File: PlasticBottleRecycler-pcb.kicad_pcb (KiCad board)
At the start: 2 copper layers, 70.9 x 56.9 mm, 33 parts, among them J1 SWIM, J2 LCD, J3 Screw_Terminal_01x04, J4 NTC, J5 HEATER, J6 FAN1, J7 +12V, J8 +5V, Q1 IRF3205, Q2 BC337, SW1 RESET, SW2 SW_Push, SW3 SW_Push, SW4 SW_Push, U1 STM8S005K6T6C, U2 AMS1117

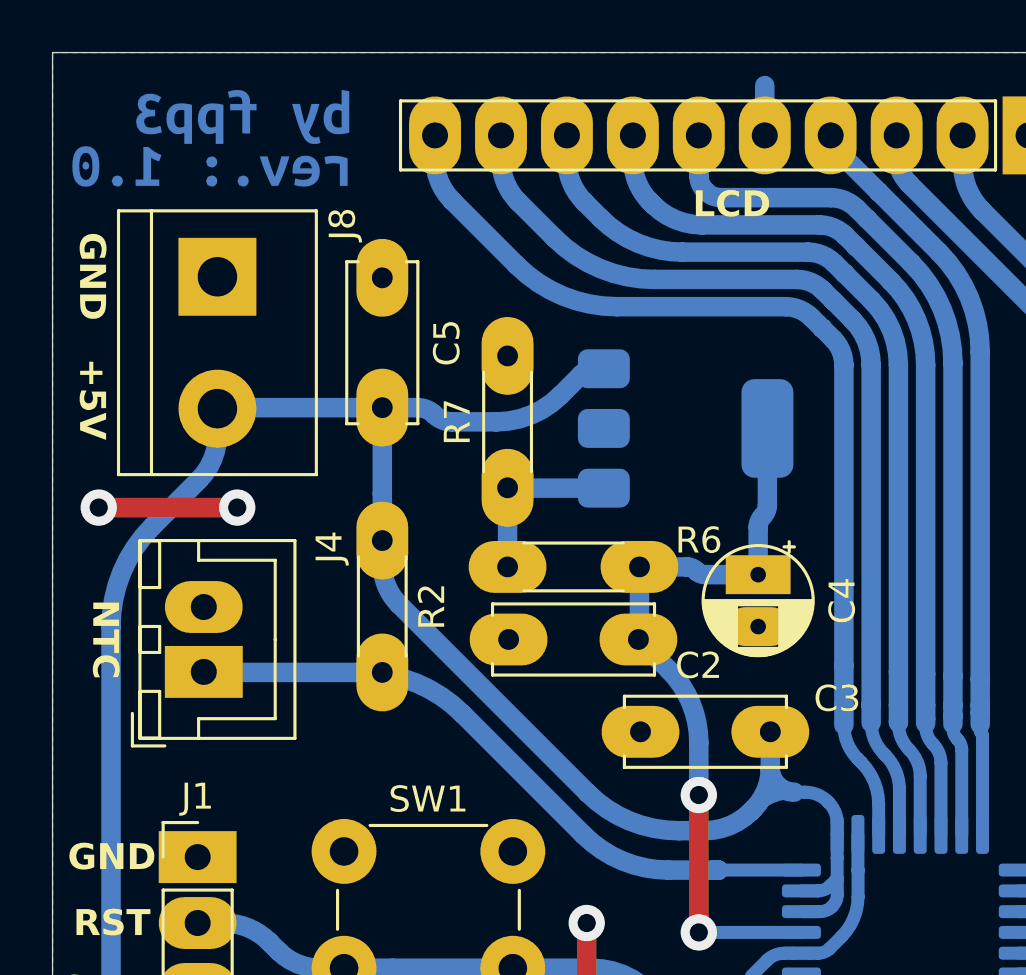
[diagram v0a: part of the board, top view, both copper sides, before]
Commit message: Remove unnecesary voltage regulator
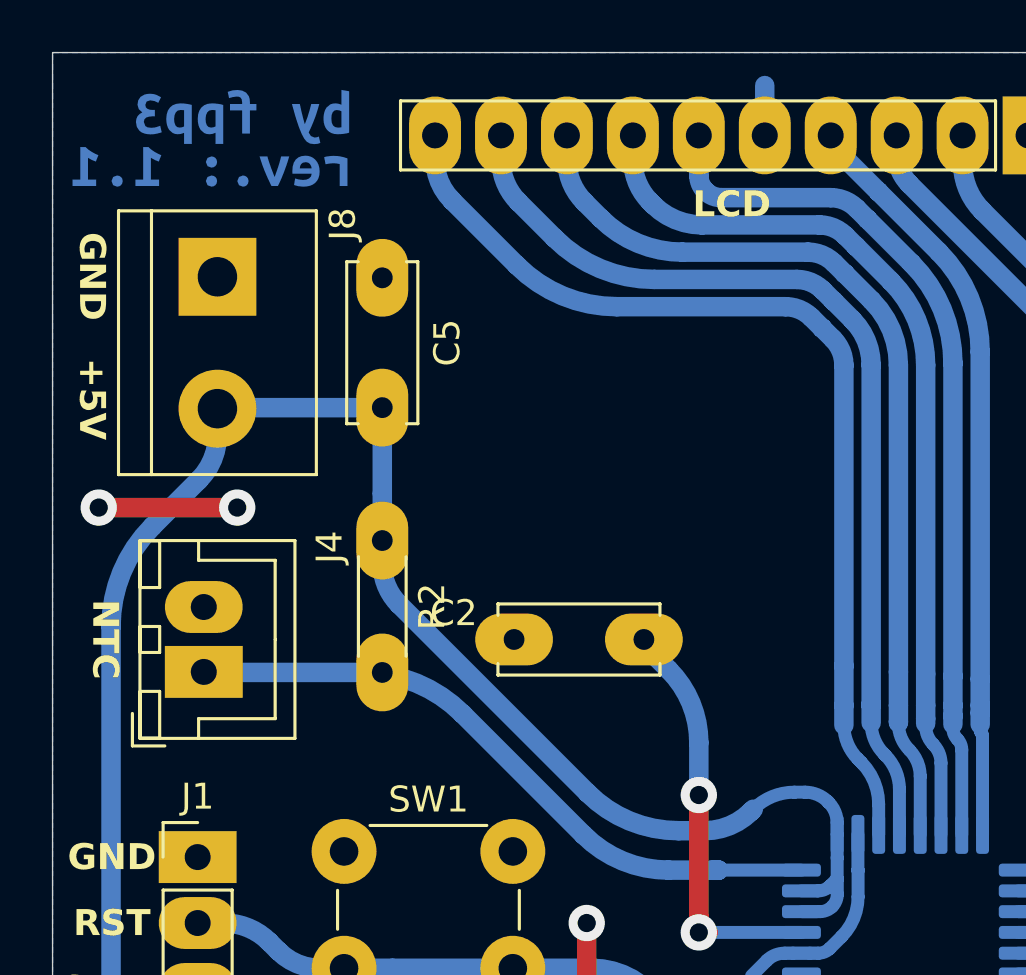
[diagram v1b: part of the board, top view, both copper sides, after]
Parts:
- removed C3: 100n, Capacitor_THT:C_Disc_D6.0mm_W2.5mm_P5.00mm
- removed C4: 10u, Capacitor_THT:CP_Radial_D4.0mm_P2.00mm
- removed R6: 10K, Resistor_THT:R_Axial_DIN0204_L3.6mm_D1.6mm_P5.08mm_Horizontal
- removed R7: 4K7, Resistor_THT:R_Axial_DIN0204_L3.6mm_D1.6mm_P5.08mm_Horizontal
- removed U2: AMS1117, Package_TO_SOT_SMD:SOT-223-3_TabPin2
- removed kibuzzard-679459C7: G***, kibuzzard-679459C7
- added kibuzzard-67C1DC92: G***, kibuzzard-67C1DC92, B.Cu at (121.2, 75.4)
- moved C2 5.21 mm to (137.9, 94.7), turned to 180 degrees
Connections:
- C2 pad 1: GND -> Net-(U1-VCAP)
- C2 pad 2: +1V8 -> GND
- U1 pad 5: +1V8 -> Net-(U1-VCAP)
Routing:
- net +1V8: track 29.7 -> 0.00 mm, vias 2 -> 0
- net Net-(U1-VCAP): track 0.00 -> 15.8 mm, vias 0 -> 2
- net +5V: track 269.8 -> 256.0 mm
- net Net-(U2-ADJ): track 7.53 -> 0.00 mm

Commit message: Revision 2.0
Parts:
- removed R8: 680, Resistor_THT:R_Axial_DIN0207_L6.3mm_D2.5mm_P10.16mm_Horizontal
- removed kibuzzard-679458C4: G***, kibuzzard-679458C4
- removed kibuzzard-67C1DC92: G***, kibuzzard-67C1DC92
- added BZ1: Buzzer, Buzzer_Beeper:Buzzer_12x9.5RM7.6, F.Cu at (124.3, 140.2)
- added C3: 100nF, Capacitor_THT:C_Disc_D6.0mm_W2.5mm_P5.00mm, F.Cu at (130.9, 118.0)
- added C4: 100n, Capacitor_THT:C_Disc_D6.0mm_W2.5mm_P5.00mm, F.Cu at (138.7, 131.5)
- added H1: MountingHole, MountingHole:MountingHole_3.2mm_M3, F.Cu at (133.1, 40.9)
- added H2: MountingHole, MountingHole:MountingHole_3.2mm_M3, F.Cu at (165.5, 40.9)
- added H3: MountingHole, MountingHole:MountingHole_3.2mm_M3, F.Cu at (124.8, 79.0)
- added H4: MountingHole, MountingHole:MountingHole_3.2mm_M3, F.Cu at (173.7, 79.0)
- added J10: RUNOUT, Connector_Molex:Molex_KK-254_AE-6410-03A_1x03_P2.54mm_Vertical, F.Cu at (178.9, 150.2)
- added J11: STEPPER, Connector_JST:JST_XA_B04B-XASK-1_1x04_P2.50mm_Vertical, F.Cu at (179.7, 140.6)
- added J12: LCD, Connector_PinHeader_2.54mm:PinHeader_1x10_P2.54mm_Vertical, B.Cu at (162.5, 51.3)
- added J9: NTC, Connector_JST:JST_XH_B2B-XH-A_1x02_P2.50mm_Vertical, F.Cu at (165.3, 150.1)
- added Q3: IRF3205, Package_TO_SOT_THT:TO-220-3_Vertical, F.Cu at (162.7, 107.6)
- added R6: 10K, Resistor_THT:R_Axial_DIN0204_L3.6mm_D1.6mm_P5.08mm_Horizontal, F.Cu at (147.5, 72.3)
- added R7: 10K, Resistor_THT:R_Axial_DIN0204_L3.6mm_D1.6mm_P5.08mm_Horizontal, F.Cu at (133.9, 72.3)
- added U2: STM8S005K6T6C, Package_QFP:LQFP-32_7x7mm_P0.8mm, B.Cu at (146.9, 134.4)
- added kibuzzard-67C39444: G***, kibuzzard-67C39444, B.Cu at (117.2, 107.6)
- added kibuzzard-67C39444: G***, kibuzzard-67C39444, B.Cu at (156.7, 44.2)
- added kibuzzard-67C39452: G***, kibuzzard-67C39452, B.Cu at (117.2, 147.1)
- added kibuzzard-67C39452: G***, kibuzzard-67C39452, B.Cu at (154.4, 39.8)
- added kibuzzard-67C3947F: G***, kibuzzard-67C3947F, B.Cu at (179.8, 104.2)
- added kibuzzard-67C3B0C4: G***, kibuzzard-67C3B0C4, B.Cu at (150.1, 83.9)
- C1: value 1000u -> 330nF; footprint Capacitor_THT:CP_Radial_D10.0mm_P5.00mm -> Capacitor_THT:C_Disc_D6.0mm_W2.5mm_P5.00mm
- C2: value 100n -> 1000u; footprint Capacitor_THT:C_Disc_D6.0mm_W2.5mm_P5.00mm -> Capacitor_THT:CP_Radial_D10.0mm_P5.00mm
- J1: value SWIM -> Conn_01x08; footprint Connector_PinHeader_2.54mm:PinHeader_1x04_P2.54mm_Vertical -> Connector_Molex:Molex_KK-254_AE-6410-08A_1x08_P2.54mm_Vertical
- J2: value LCD -> Conn_01x04; footprint Connector_PinHeader_2.54mm:PinHeader_1x10_P2.54mm_Vertical -> Connector_Molex:Molex_KK-254_AE-6410-04A_1x04_P2.54mm_Vertical
- J3: value Screw_Terminal_01x04 -> Conn_01x08; footprint TerminalBlock:TerminalBlock_bornier-4_P5.08mm -> Connector_Molex:Molex_KK-254_AE-6410-08A_1x08_P2.54mm_Vertical
- J4: value NTC -> Conn_01x04; footprint Connector_JST:JST_XH_B2B-XH-A_1x02_P2.50mm_Vertical -> Connector_Molex:Molex_KK-254_AE-6410-04A_1x04_P2.54mm_Vertical
- J5: value HEATER -> SWIM; footprint TerminalBlock:TerminalBlock_bornier-2_P5.08mm -> Connector_PinHeader_2.54mm:PinHeader_1x04_P2.54mm_Vertical
- J6: value FAN1 -> +12V; footprint Connector_PinHeader_2.54mm:PinHeader_1x02_P2.54mm_Vertical -> TerminalBlock:TerminalBlock_bornier-2_P5.08mm
- J7: value +12V -> FAN1; footprint TerminalBlock:TerminalBlock_bornier-2_P5.08mm -> Connector_Molex:Molex_KK-254_AE-6410-03A_1x03_P2.54mm_Vertical
- J8: value +5V -> HEATER
- Q1: value IRF3205 -> BC337; footprint PCM_Package_TO_SOT_THT_AKL:TO-220-3_Vertical_GDS -> Package_TO_SOT_THT:TO-92L_Inline_Wide
- Q2: footprint PCM_Package_TO_SOT_THT_AKL:TO-92_Inline_Wide_CBE -> Package_TO_SOT_THT:TO-92L_Inline_Wide
- R1: value 10K -> 680
- R2: value 4K7 -> 680
- R4: value 10K -> 4K7
- SW1: footprint Button_Switch_THT:SW_PUSH_6mm_H5mm -> Button_Switch_THT:SW_Tactile_SPST_Angled_PTS645Vx39-2LFS
- SW2: value SW_Push -> BTN_PLUS; footprint Button_Switch_THT:SW_PUSH_6mm_H5mm -> Button_Switch_THT:SW_PUSH_6mm_H7.3mm; moved to B.Cu
- SW3: value SW_Push -> BTN_OK; footprint Button_Switch_THT:SW_PUSH_6mm_H5mm -> Button_Switch_THT:SW_PUSH_6mm_H7.3mm; moved to B.Cu
- SW4: value SW_Push -> BTN_MINUS; footprint Button_Switch_THT:SW_PUSH_6mm_H5mm -> Button_Switch_THT:SW_PUSH_6mm_H7.3mm; moved to B.Cu
- U1: value STM8S005K6T6C -> LM7805_TO220; footprint Package_QFP:LQFP-32_7x7mm_P0.8mm -> Package_TO_SOT_THT:TO-92L_Inline_Wide; moved to F.Cu
- moved Q1 80.8 mm to (134.8, 152.4), turned to 90 degrees
- moved J8 69.8 mm to (179.2, 120.1)
- moved J5 68.0 mm to (119.4, 113.8), turned to 0 degrees
- moved J7 59.5 mm to (158.6, 150.2), turned to 180 degrees
- moved R2 58.4 mm to (142.9, 147.3)
- moved R5 56.4 mm to (159.6, 72.2)
- moved SW2 48.4 mm to (166.1, 76.8), turned to 180 degrees
- moved SW3 47.2 mm to (152.7, 76.7), turned to 180 degrees
- moved J3 46.6 mm to (134.5, 107.2), turned to 0 degrees
- moved J1 46.3 mm to (134.6, 58.9)
- moved SW4 46.0 mm to (138.9, 76.7), turned to 180 degrees
- moved C5 44.9 mm to (141.7, 123.5)
- moved C1 42.7 mm to (136.0, 118.0)
- moved R1 38.5 mm to (139.3, 147.3), turned to -90 degrees
- moved Q2 36.7 mm to (148.2, 152.4)
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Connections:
- A1 pad 1: GND -> /Controller Board/GND
- A1 pad 10: A4988_MS1 -> /Controller Board/A4988_MS1
- A1 pad 11: A4988_MS2 -> /Controller Board/A4988_MS2
- A1 pad 12: A4988_MS3 -> /Controller Board/A4988_MS3
- A1 pad 13: +5V -> /Controller Board/+5V
- A1 pad 14: A4988_SLP -> /Controller Board/A4988_SLP
- A1 pad 15: A4988_STP -> /Controller Board/A4988_STP
- A1 pad 16: A4988_DIR -> /Controller Board/A4988_DIR
- A1 pad 2: +5V -> /Controller Board/+5V
- A1 pad 7: GND -> /Controller Board/GND
- A1 pad 8: +12V -> /Controller Board/+12V
- A1 pad 9: A4988_ENA -> /Controller Board/A4988_ENA
- C1 pad 1: +12V -> /Controller Board/+12V
- C1 pad 2: GND -> /Controller Board/GND
- C2 pad 1: Net-(U1-VCAP) -> /Controller Board/+12V
- C2 pad 2: GND -> /Controller Board/GND
- C5 pad 1: GND -> /Controller Board/GND
- C5 pad 2: +5V -> /Controller Board/+5V
- J1 pad 1: GND -> /IO Board/GND
- J1 pad 2: RESET -> /IO Board/+5V
- J1 pad 3: SWIM -> /IO Board/LCD_D7
- J1 pad 4: +5V -> /IO Board/LCD_D6
- J2 pad 1: GND -> /IO Board/GND
- J2 pad 2: +5V -> /IO Board/BTN_PLUS
- J2 pad 3: Net-(J2-Pin_3) -> /IO Board/BTN_OK
- J2 pad 4: LCD_RS -> /IO Board/BTN_MINUS
- J3 pad 1: Net-(A1-1B) -> /Controller Board/GND
- J3 pad 2: Net-(A1-1A) -> /Controller Board/+5V
- J3 pad 3: Net-(A1-2A) -> /Controller Board/LCD_D7
- J3 pad 4: Net-(A1-2B) -> /Controller Board/LCD_D6
- J4 pad 1: Net-(J4-Pin_1) -> /Controller Board/GND
- J4 pad 2: GND -> /Controller Board/BTN_PLUS
- J5 pad 1: Net-(J5-Pin_1) -> /Controller Board/GND
- J5 pad 2: +12V -> /Controller Board/RESET
- J6 pad 1: Net-(J6-Pin_1) -> /Controller Board/GND
- J6 pad 2: +12V -> /Controller Board/+12V
- J7 pad 1: GND -> Net-(J7-Pin_1)
- J7 pad 2: +12V -> /Controller Board/+12V
- J8 pad 1: GND -> Net-(J8-Pin_1)
- J8 pad 2: +5V -> /Controller Board/+12V
- Q1 pad 1: HEATER -> Net-(BZ1--)
- Q1 pad 2: Net-(J5-Pin_1) -> Net-(Q1-B)
- Q1 pad 3: GND -> /Controller Board/GND
- Q2 pad 1: Net-(J6-Pin_1) -> Net-(J7-Pin_1)
- Q2 pad 3: GND -> /Controller Board/GND
- R1 pad 1: +5V -> /Controller Board/BUZZER
- R1 pad 2: RESET -> Net-(Q1-B)
- R2 pad 1: +5V -> /Controller Board/FAN1
- R2 pad 2: Net-(J4-Pin_1) -> Net-(Q2-B)
- R3 pad 1: BTN_PLUS -> /Controller Board/+5V
- R3 pad 2: GND -> /Controller Board/RESET
- R4 pad 1: GND -> /Controller Board/+5V
- R4 pad 2: BTN_OK -> Net-(J9-Pin_1)
- R5 pad 1: GND -> /IO Board/BTN_PLUS
- R5 pad 2: BTN_MINUS -> /IO Board/GND
- RV1 pad 1: +5V -> /IO Board/+5V
- RV1 pad 2: Net-(J2-Pin_3) -> Net-(J12-Pin_3)
- RV1 pad 3: GND -> /IO Board/GND
- SW1 pad 1: GND -> /Controller Board/GND
- SW1 pad 2: RESET -> /Controller Board/RESET
- SW2 pad 1: BTN_PLUS -> /IO Board/BTN_PLUS
- SW2 pad 2: +5V -> /IO Board/+5V
- SW3 pad 1: BTN_OK -> /IO Board/BTN_OK
- SW3 pad 2: +5V -> /IO Board/+5V
- SW4 pad 1: BTN_MINUS -> /IO Board/BTN_MINUS
- SW4 pad 2: +5V -> /IO Board/+5V
- U1 pad 1: RESET -> /Controller Board/+12V
- U1 pad 2: unconnected-(U1-PA1/OSCIN-Pad2) -> /Controller Board/GND
- U1 pad 3: unconnected-(U1-PA2/OSCOUT-Pad3) -> /Controller Board/+5V
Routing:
- net +5V: track 256.0 -> 0.00 mm, vias 2 -> 0
- net /Controller Board/+12V: track 0.00 -> 157.0 mm, vias 0 -> 4
- net /Controller Board/+5V: track 0.00 -> 129.1 mm, vias 0 -> 4
- net /IO Board/+5V: track 0.00 -> 104.3 mm
- net SWIM: track 97.5 -> 0.00 mm
- net +12V: track 76.0 -> 0.00 mm
- net /Controller Board/HEATER: track 0.00 -> 65.8 mm, vias 0 -> 4
- net HEATER: track 58.5 -> 0.00 mm, vias 2 -> 0
- net Net-(J9-Pin_1): track 0.00 -> 55.8 mm, vias 0 -> 4
- net /Controller Board/SWIM: track 0.00 -> 51.9 mm, vias 0 -> 2
- net /Controller Board/BTN_PLUS: track 0.00 -> 48.8 mm
- net /Controller Board/RESET: track 0.00 -> 48.3 mm, vias 0 -> 2
- net /Controller Board/BTN_OK: track 0.00 -> 45.4 mm
- net /Controller Board/BTN_MINUS: track 0.00 -> 41.4 mm
- net LCD_D7: track 38.8 -> 0.00 mm
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- added copper zone on B.Cu, net /Controller Board/GND
- added copper zone on B.Cu, net /IO Board/GND
- removed copper zone on B.Cu, net GND
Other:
- board size 70.9 x 56.9 mm -> 69.8 x 118.9 mm
- board text removed: "+5V"
- board text removed: "1B 1A 2A 2B"
- board text removed: "GND"
- board text removed: "GND +12V"
- board text removed: "GND +12V FAN"
- board text removed: "GND +5V"
- board text removed: "HEATER"
- board text removed: "MINUS"
- board text removed: "NTC"
- board text removed: "OK"
- board text removed: "PLUS"
- board text removed: "RST"
- board text removed: "SWM"

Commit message: Minor Changes
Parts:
- moved C2 2.11 mm to (161.3, 118.7)
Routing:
- net /Controller Board/GND: track 26.8 -> 37.6 mm, vias 4 -> 6
- net /Controller Board/HEATER: track 65.8 -> 75.0 mm
- net /Controller Board/+5V: track 129.1 -> 130.7 mm
- net /Controller Board/+12V: track 157.0 -> 156.0 mm
- net /IO Board/BTN_MINUS: track 21.3 -> 20.6 mm

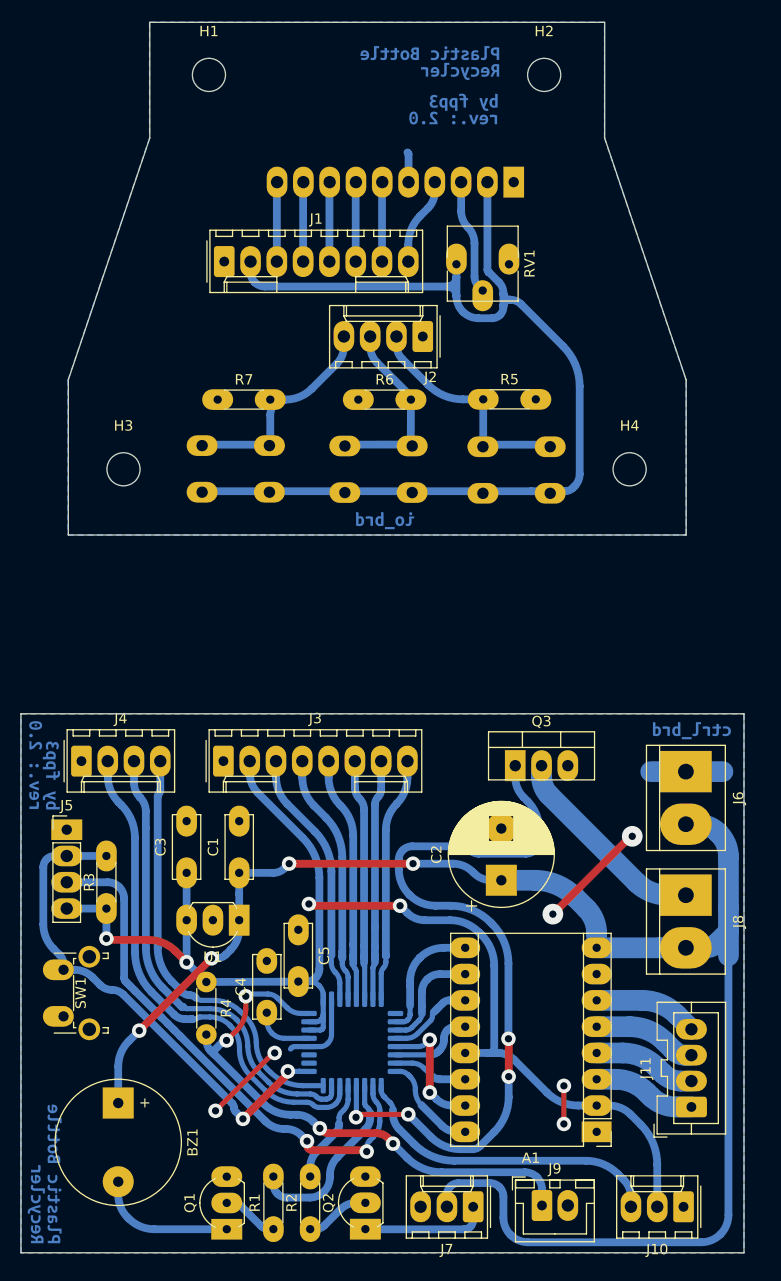
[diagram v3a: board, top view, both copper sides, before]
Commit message: Restored pad copper layers to "all layers"
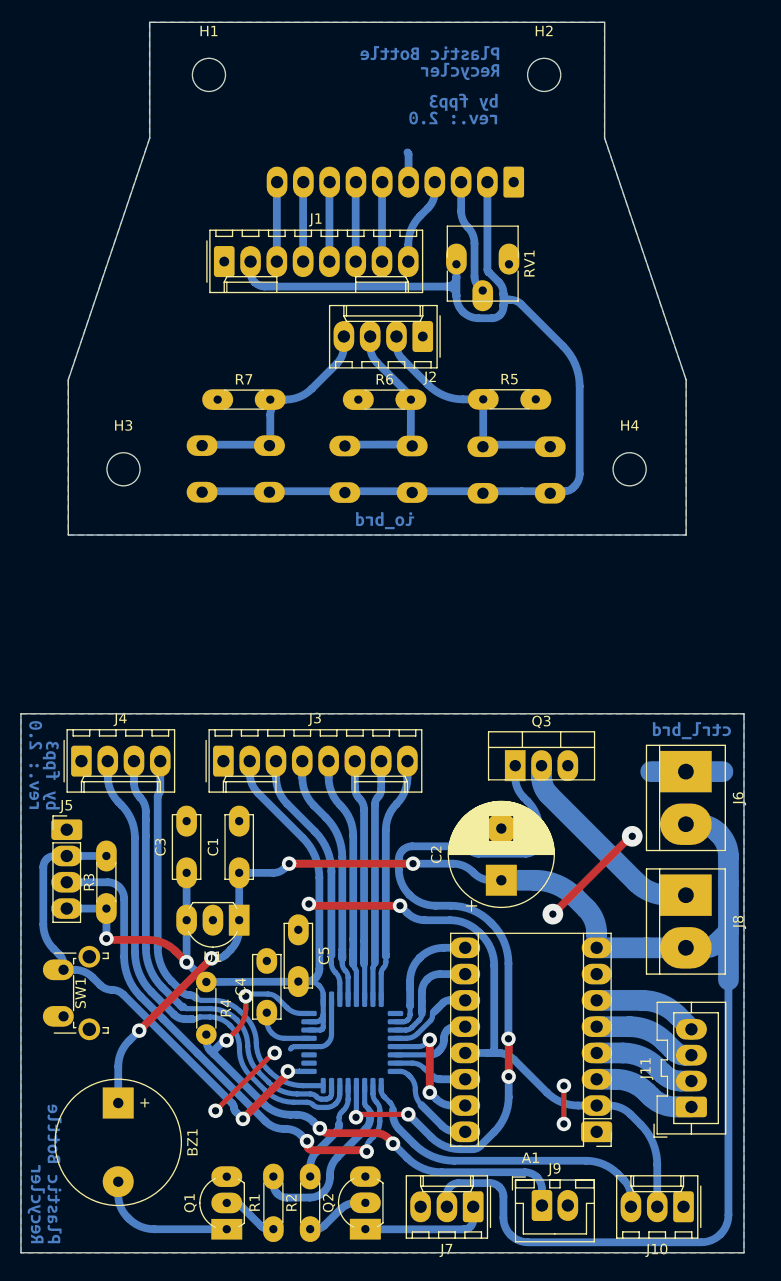
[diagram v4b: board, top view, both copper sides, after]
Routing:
- net /Controller Board/GND: track 37.6 -> 36.9 mm
